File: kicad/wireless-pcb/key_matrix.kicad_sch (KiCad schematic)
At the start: 42 parts, among them SW1 EC_SW, SW10 EC_SW, SW11 EC_SW, SW12 EC_SW, SW13 EC_SW, SW14 EC_SW, SW15 EC_SW, SW2 EC_SW, SW3 EC_SW, SW35 SW_Push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

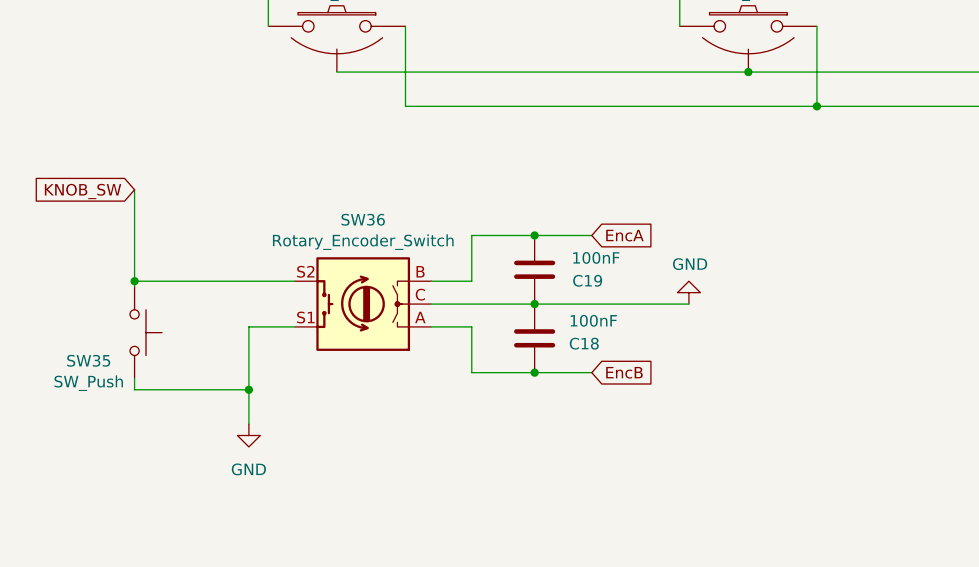
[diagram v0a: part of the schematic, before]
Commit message: Various cleanup, better pin selection, etc.
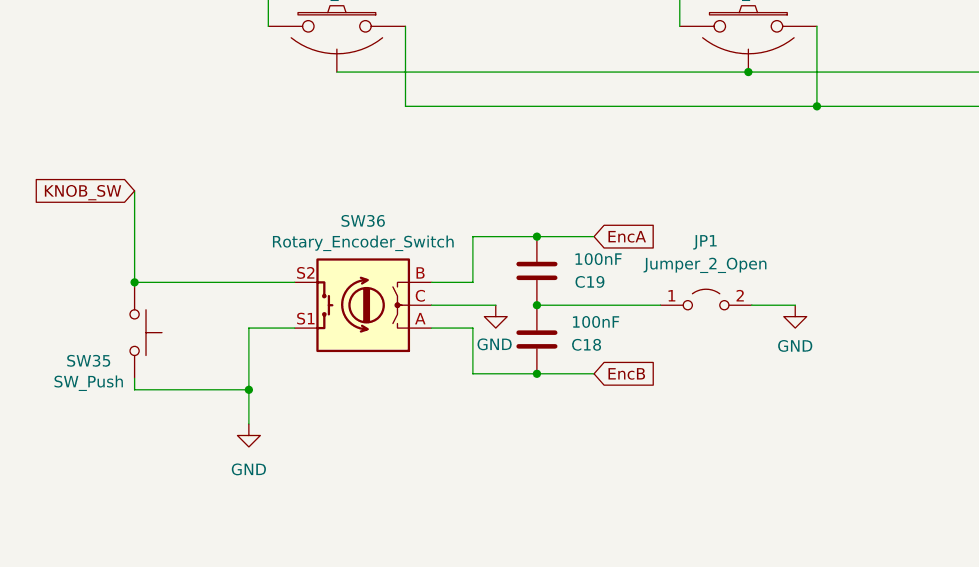
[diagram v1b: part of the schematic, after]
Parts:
- added JP1: Jumper_2_Open, Jumper:SolderJumper-2_P1.3mm_Open_RoundedPad1.0x1.5mm, symbol Jumper:Jumper_2_Open
- SW3, SW35: now left out of the parts list
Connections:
- net GND: now also JP1.2 (B); no longer C18.2, C19.2
- new net: C18.2, C19.2, JP1.1 (A)

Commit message: BOM tweaks, add some test points, minor placement tweaks.
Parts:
- JP1, SW3: now left out of the parts list
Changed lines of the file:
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@@
   )
   (symbol (lib_id "Jumper:Jumper_2_Open") (at 106.426 127.508 0) (unit 1)
-    (in_bom yes) (on_board yes) (dnp no) (fields_autoplaced)
+    (in_bom no) (on_board yes) (dnp no) (fields_autoplaced)
     (property "Reference" "JP1" (at 106.426 120.396 0)
       (effects (font (size 1.27 1.27)))
@@
   )
   (symbol (lib_id "cipulot_parts:EC_SW") (at 231.14 147.32 0) (unit 1)
-    (in_bom yes) (on_board yes) (dnp no)
+    (in_bom no) (on_board yes) (dnp no)
     (property "Reference" "SW3" (at 231.14 140.97 0)
       (effects (font (size 1.27 1.27)))
@@
   )
   (symbol (lib_id "cipulot_parts:EC_SW") (at 193.04 147.32 0) (mirror y) (unit 1)
-    (in_bom yes) (on_board yes) (dnp no)
+    (in_bom no) (on_board yes) (dnp no)
     (property "Reference" "SW3" (at 193.04 140.97 0)
       (effects (font (size 1.27 1.27)))
@@
   )
   (symbol (lib_id "cipulot_parts:EC_SW") (at 175.26 147.32 0) (mirror y) (unit 1)
-    (in_bom yes) (on_board yes) (dnp no)
+    (in_bom no) (on_board yes) (dnp no)
     (property "Reference" "SW3" (at 175.26 140.97 0)
       (effects (font (size 1.27 1.27)))
@@
   )
   (symbol (lib_id "cipulot_parts:EC_SW") (at 213.36 147.32 0) (unit 1)
-    (in_bom yes) (on_board yes) (dnp no)
+    (in_bom no) (on_board yes) (dnp no)
     (property "Reference" "SW3" (at 213.36 140.97 0)
       (effects (font (size 1.27 1.27)))
